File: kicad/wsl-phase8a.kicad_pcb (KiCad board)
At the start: 2 copper layers, 100 x 100 mm, 60 parts, among them J1 5.08mm 2P TB, J10 5.08mm 2P TB, J11 5.08mm 2P TB, J2 5.08mm 2P TB, J3 5.08mm 2P TB, J4 5.08mm 2P TB, J5 5.08mm 2P TB, J6 5.08mm 2P TB, J7 5.08mm 2P TB, J8 5.08mm 2P TB, J9 5.08mm 2P TB, Q1 AO3400A, Q2 AO3400A, U1 NE555

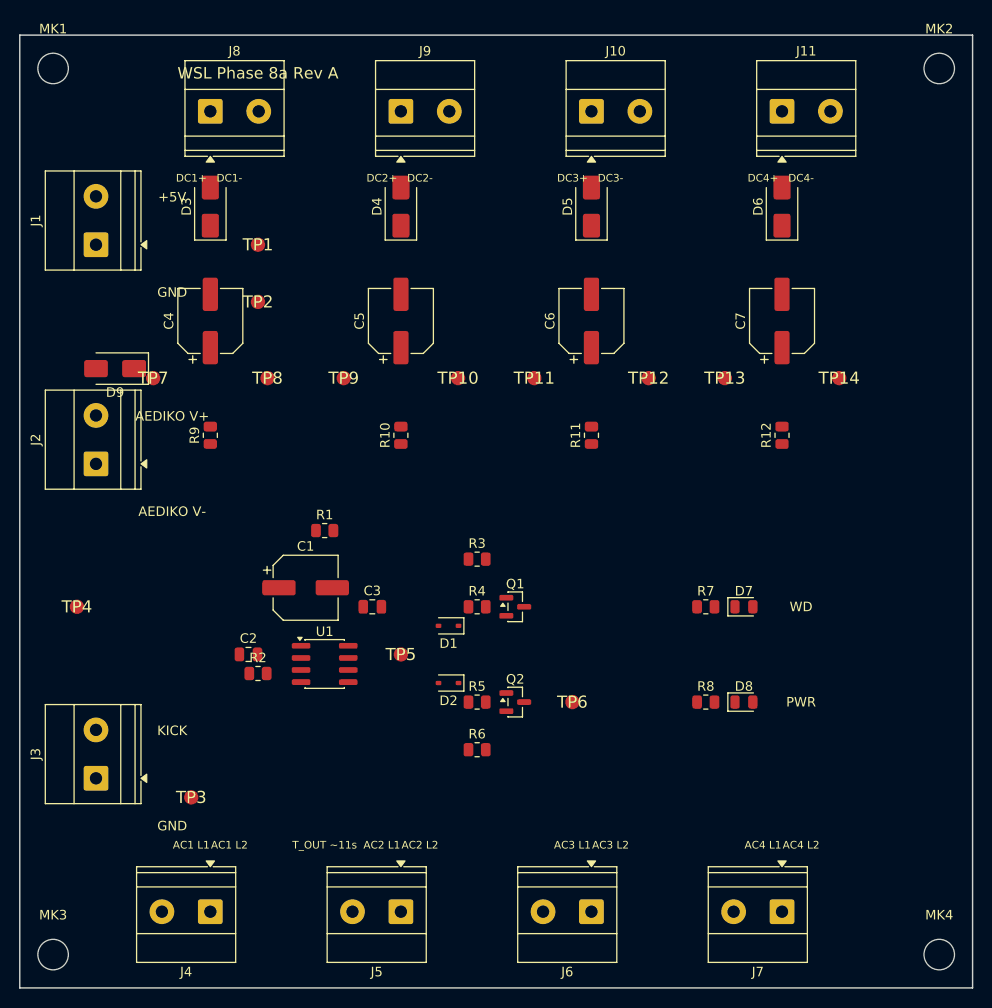
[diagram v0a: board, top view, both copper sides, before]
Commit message: Clean regen with proper TestPoint FPID + delete stale DSN/SES
Previous .ses import undid the C2 and D9 placement fixes because the
.ses file contained (place X y z) lines with the old positions. Need
to do a full DSN → autoroute → SES cycle from the CURRENT placement,
not import the stale .ses.

Also fixed test pad FPID: FootprintLoad sets only the footprint name
without the library prefix ('TestPoint_Pad_1.5x1.5mm'), which still
doesn't survive DSN export. Added explicit SetFPID with the full
'TestPoint:TestPoint_Pad_1.5x1.5mm' library:name form.

Deleted stale .dsn and .ses to force a fresh export on next run.

Co-Authored-By: Claude Opus 4.7 (1M context) <noreply@anthropic.com>
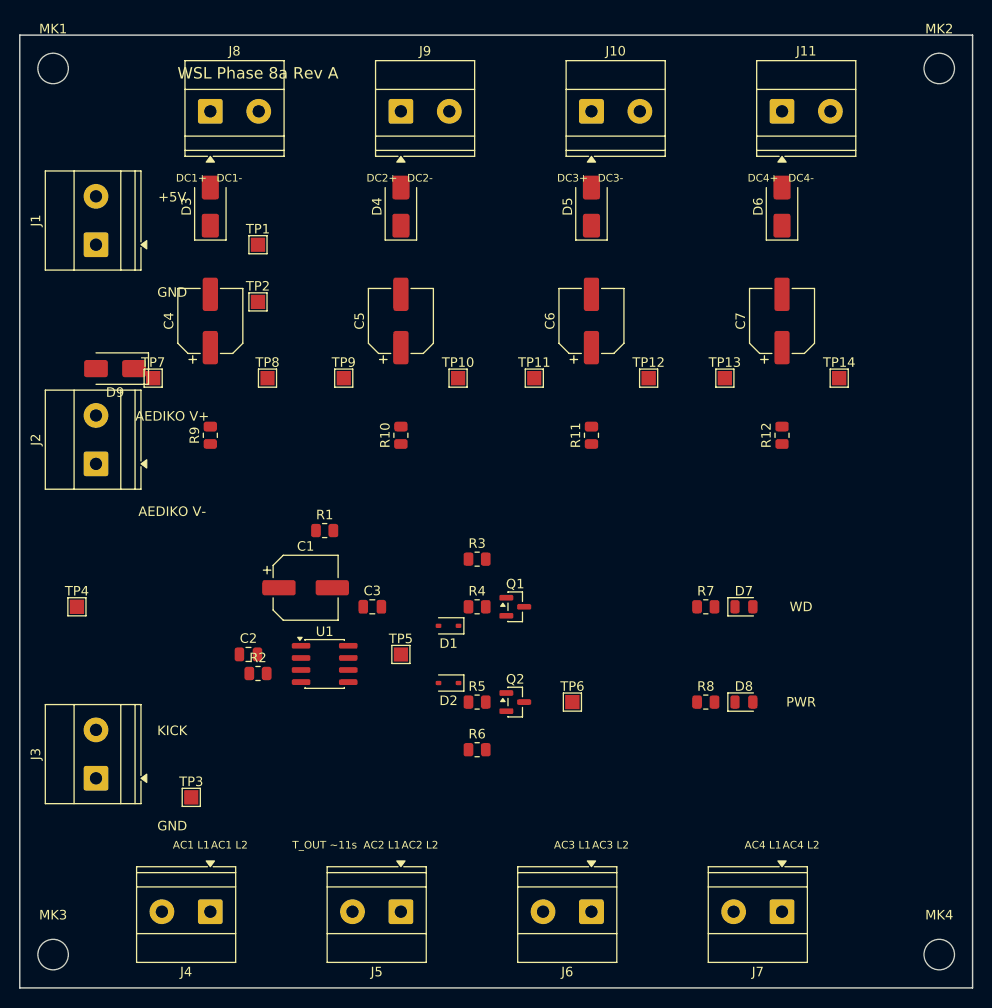
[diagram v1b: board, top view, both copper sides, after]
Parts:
- TP1, TP10, TP11, TP12, TP13, TP14, TP2, TP3, TP4, TP5, TP6, TP7, TP8, TP9: footprint custom:test_pad_1.5mm -> TestPoint:TestPoint_Pad_1.5x1.5mm

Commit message: Move channel test pads to y=48 to clear D9/J2 conflict
After D9 moved to (10, 35), TP7 at (14, 36) ended up 0mm from D9.pad1
(VCC_5V) — DRC short error. Same area had TP7 ↔ J2 courtyard overlap.

Moved all 8 channel test pads (TP7-TP14) from y=36 to y=48. That y
range is the clean gap between AC bleeders R9-R12 at y=42 and the
watchdog cluster starting at y=55+. Plenty of clearance to nearby
components.

x-positions tweaked from (14, 26, 34, 46, 54, 66, 74, 86) to
(15, 25, 35, 45, 55, 65, 75, 85) — round numbers, evenly spaced.

Co-Authored-By: Claude Opus 4.7 (1M context) <noreply@anthropic.com>
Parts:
- moved TP10 12.0 mm to (45.0, 48.0)
- moved TP11 12.0 mm to (55.0, 48.0)
- moved TP12 12.0 mm to (65.0, 48.0)
- moved TP13 12.0 mm to (75.0, 48.0)
- moved TP14 12.0 mm to (85.0, 48.0)
- moved TP7 12.0 mm to (15.0, 48.0)
- moved TP8 12.0 mm to (25.0, 48.0)
- moved TP9 12.0 mm to (35.0, 48.0)

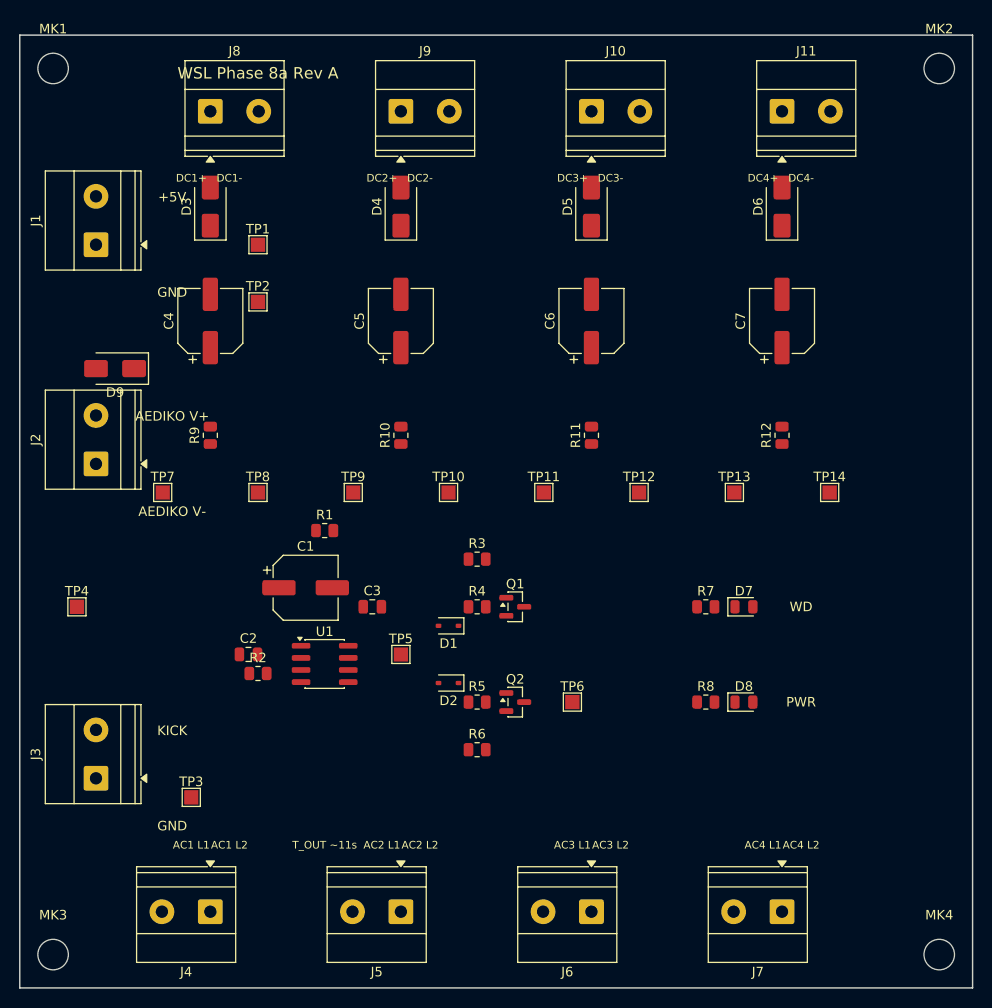
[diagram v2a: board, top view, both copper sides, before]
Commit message: Silkscreen polish: consolidate per-pin labels to per-channel
Was 26 labels with many pairs too close together (KiCad's silk-min-width
constraint flagged AC1 L1/L2, AC2 L1/L2, etc. for being 4mm apart when
5mm is the minimum). Title and power-terminal labels were overlapping
J1/J2/J8 footprint outlines too.

Cut to 13 labels:
- Removed individual DC1+ / DC1- / AC1 L1 / AC1 L2 pairs
- Replaced with single 'CH1 DC' (top) and 'CH1 24VAC' (bottom) labels
  per channel — pin numbers on the terminal outline already show polarity
- Consolidated power terminal labels: '+5V/GND', 'AEDIKO', 'KICK/GND'
  next to J1, J2, J3 (was 6 separate labels for the 3 terminals)
- Removed 'WSL Phase 8a Rev A' title (was overlapping J8) and the
  'T_OUT ~11s' service note (overlapping U1 area)

Expected DRC reduction: 22 -> ~5 warnings (a few residual silk_over_copper
warnings on test pad refdes will remain, those are unavoidable for the
TestPoint footprint since the refdes sits over its own pad).

Co-Authored-By: Claude Opus 4.7 (1M context) <noreply@anthropic.com>
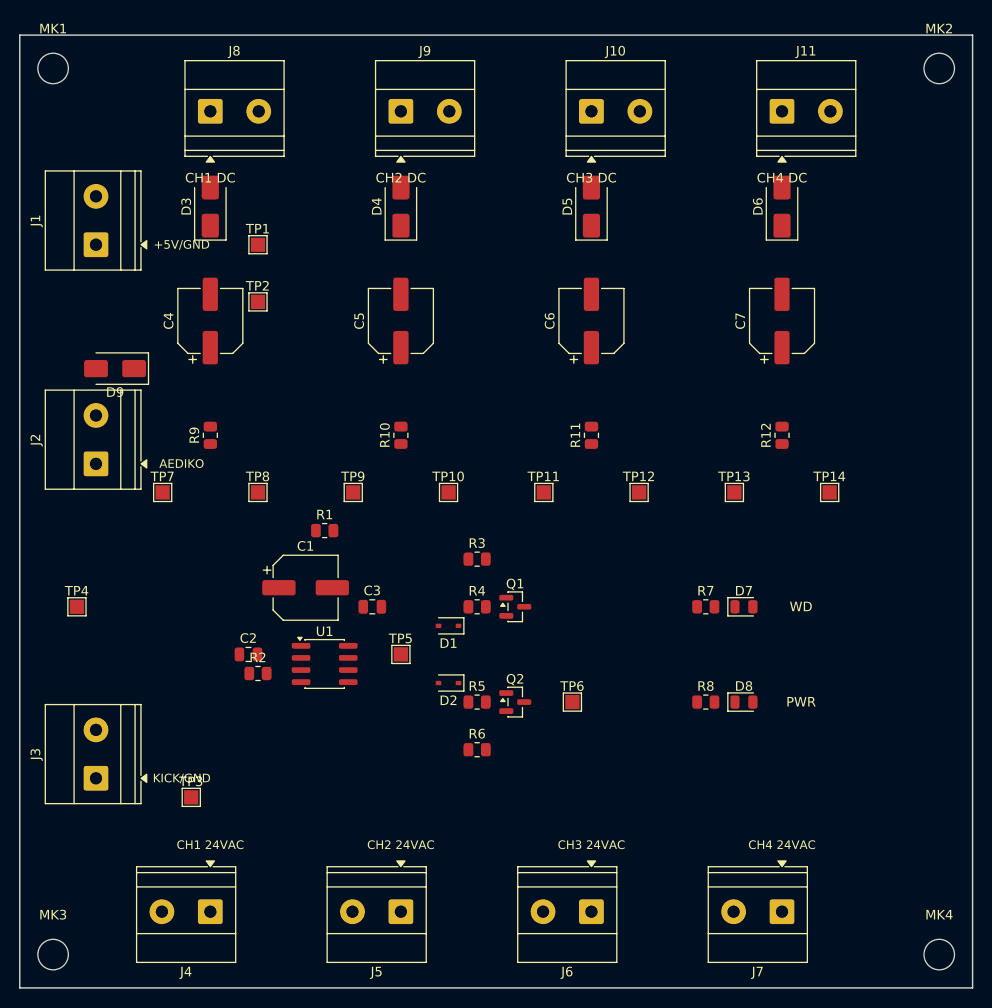
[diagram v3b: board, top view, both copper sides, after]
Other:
- board text added: "+5V/GND"
- board text added: "AEDIKO"
- board text added: "CH1 24VAC"
- board text added: "CH1 DC"
- board text added: "CH2 24VAC"
- board text added: "CH2 DC"
- board text added: "CH3 24VAC"
- board text added: "CH3 DC"
- board text added: "CH4 24VAC"
- board text added: "CH4 DC"
- board text added: "KICK/GND"
- board text removed: "+5V"
- board text removed: "AC1 L1"
- board text removed: "AC1 L2"
- board text removed: "AC2 L1"
- board text removed: "AC2 L2"
- board text removed: "AC3 L1"
- board text removed: "AC3 L2"
- board text removed: "AC4 L1"
- board text removed: "AC4 L2"
- board text removed: "AEDIKO V+"
- board text removed: "AEDIKO V-"
- board text removed: "DC1+"
- board text removed: "DC1-"
- board text removed: "DC2+"
- board text removed: "DC2-"
- board text removed: "DC3+"
- board text removed: "DC3-"
- board text removed: "DC4+"
- board text removed: "DC4-"
- board text removed: "GND"
- board text removed: "KICK"
- board text removed: "T_OUT ~11s"
- board text removed: "WSL Phase 8a Rev A"

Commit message: Add U1.pin8 -> C2.pin1 VCC track FreeRouting missed
FreeRouting routed VCC_5V to all pads except U1.pin8, leaving the
NE555's VCC pin unconnected. Single DRC error, otherwise board is
clean.

scripts/fix_u1_vcc.py adds a 3-segment L-shaped track on F.Cu at
0.5mm width (Power net class):
  U1.pin8 (34.475, 64.095)
   -> UP to (34.475, 62.0)         [clears U1 body top at y=63.55]
   -> LEFT to (23.05, 62.0)        [horizontal above U1]
   -> DOWN to C2.pin1 (23.05, 65)  [tied into existing VCC net]

Operates on the routed .kicad_pcb directly; does not regen or wipe
FreeRouting's traces.

Co-Authored-By: Claude Opus 4.7 (1M context) <noreply@anthropic.com>
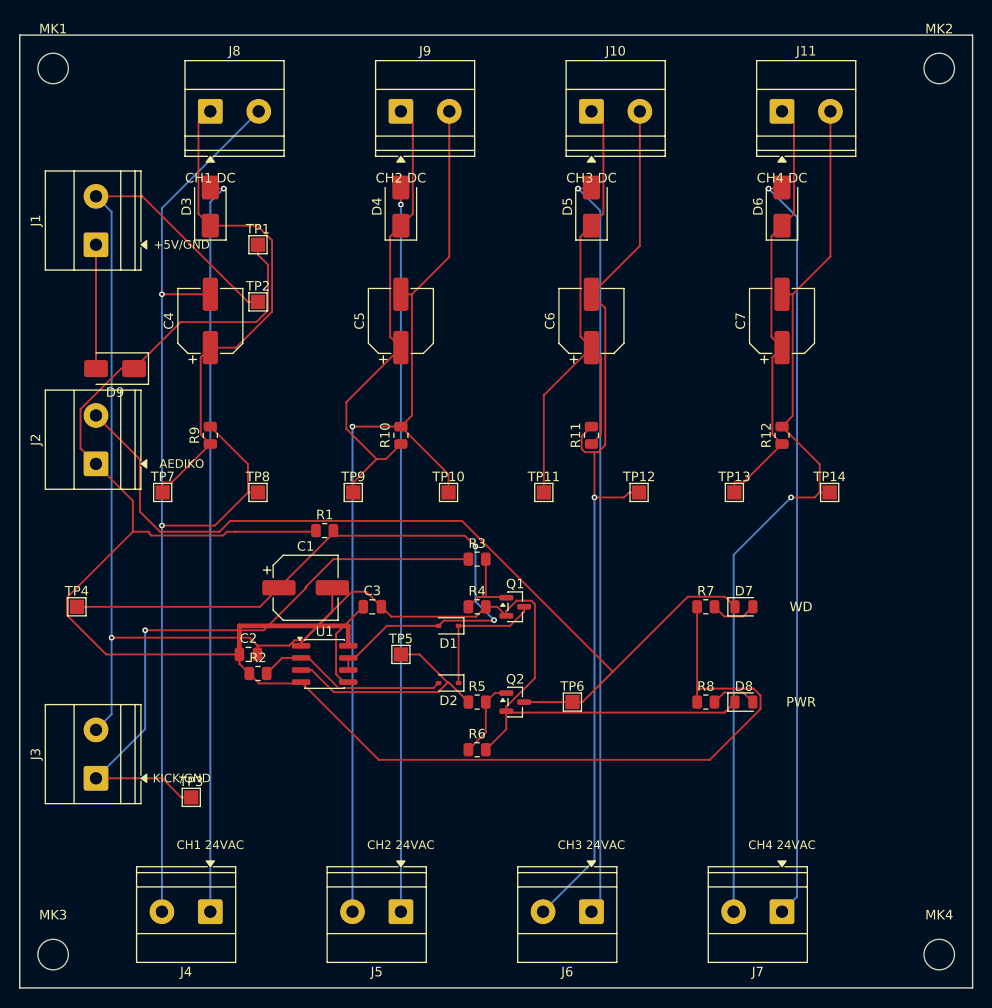
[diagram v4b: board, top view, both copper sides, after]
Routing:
- net VCC_5V: track 0.00 -> 194.7 mm
- net GND: track 0.00 -> 179.3 mm, vias 0 -> 1
- net CH1_RETURN: track 0.00 -> 113.4 mm, vias 0 -> 2
- net CH2_RETURN: track 0.00 -> 101.3 mm, vias 0 -> 1
- net CH3_RETURN: track 0.00 -> 98.8 mm, vias 0 -> 1
- net COIL_GND_RETURN: track 0.00 -> 96.7 mm
- net CH4_RETURN: track 0.00 -> 95.1 mm, vias 0 -> 1
- net AC_CH4_L1: track 0.00 -> 79.2 mm, vias 0 -> 1
- net AC_CH3_L1: track 0.00 -> 78.7 mm, vias 0 -> 1
- net AC_CH1_L1: track 0.00 -> 77.9 mm, vias 0 -> 1
- net AC_CH2_L1: track 0.00 -> 76.0 mm, vias 0 -> 1
- net TIMING_NODE: track 0.00 -> 72.7 mm, vias 0 -> 2
- net KICK: track 0.00 -> 65.6 mm, vias 0 -> 1
- net DC_CH3_POS: track 0.00 -> 55.0 mm
- net DC_CH1_POS: track 0.00 -> 54.4 mm
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
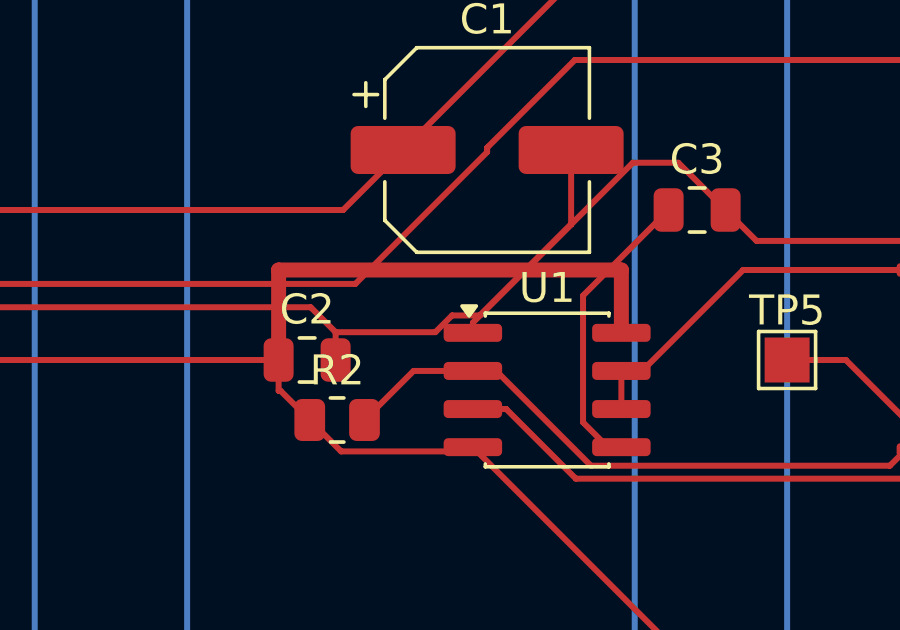
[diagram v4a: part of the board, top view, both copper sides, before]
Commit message: Remove bad U1.pin8 VCC tracks; manual interactive route needed
My fix_u1_vcc.py routed VCC at y=62 which crossed multiple existing
F.Cu traces (KICK, GND, NE555_CTRL — all run through that y range).
Added 7 new DRC errors. Programmatic routing without knowing the
existing trace layout is unsafe; KiCad's push-and-shove interactive
router handles obstacles correctly.

undo_u1_vcc_fix.py removes the 3 bad track segments by matching their
endpoint coordinates exactly. Board back to its state from FreeRouting
import (1 unconnected error: U1.pin8 VCC).

Next: manual route in KiCad with X tool.

Co-Authored-By: Claude Opus 4.7 (1M context) <noreply@anthropic.com>
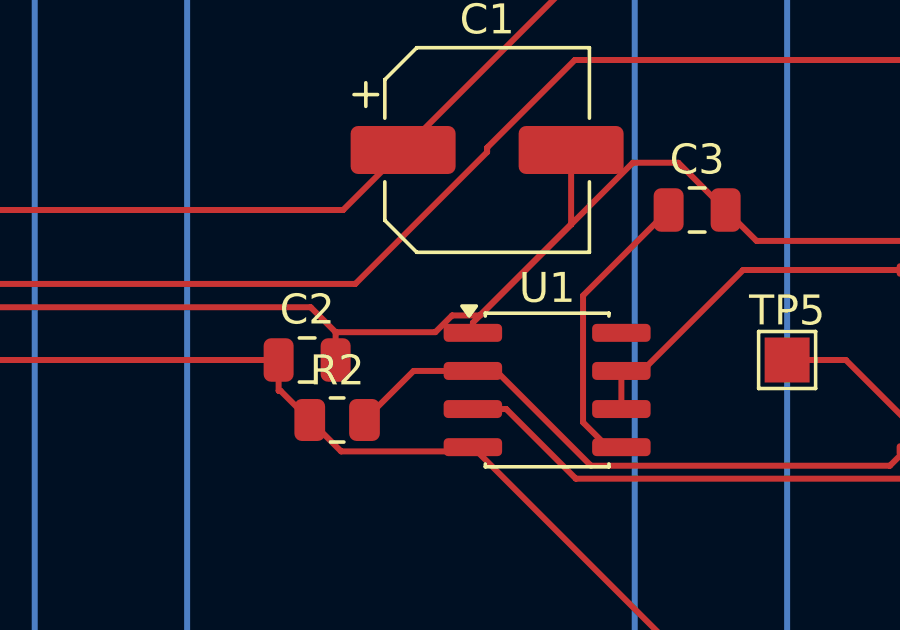
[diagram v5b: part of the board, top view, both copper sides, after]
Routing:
- net VCC_5V: track 194.7 -> 178.1 mm
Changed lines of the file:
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@@
-	)
-	(segment
-		(start 34.475 64.095)
-		(end 34.475 62)
-		(width 0.5)
-		(layer "F.Cu")
-		(net "VCC_5V")
 	)
 	(segment
@@
 		(end 29.525 67.905)
 		(width 0.2)
-		(layer "F.Cu")
-		(net "VCC_5V")
-	)
-	(segment
-		(start 34.475 62)
-		(end 23.05 62)
-		(width 0.5)
 		(layer "F.Cu")
 		(net "VCC_5V")
@@
 		(layer "F.Cu")
 		(net "VCC_5V")
-	)
-	(segment
-		(start 23.05 62)
-		(end 23.05 65)
-		(width 0.5)
-		(layer "F.Cu")
-		(net "VCC_5V")

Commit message: rev-C respin + board-#1 bring-up + 2026-06-27 machine metering + Fable review
- relay footprint root-cause fix in generate_kicad_netlist_revB.py (coil 2&5 /
  COM 1 / NO 3 / NC 4 unused, bench-metered) + full PCB toolchain + fab tree
  as ordered at JLCPCB (qty 5)
- rev-B board #1 bench bring-up docs, test packets, rev-C change list +
  readiness checklist (gates G1-G5)
- Section F machine-harness spec, metering guide, device location guide
- at-machine metering results: SC=C2A-U, TB=interlock-only (no cavity),
  N=motion-cam common, grippers GS1-7,9,10 cavities, PBZ=EE, BS=CC
- Fable review 2026-06-27: 62 verified findings incl. CRITICAL J_SAFETY
  TB/SC loop unbuildable as measured (docs/phase8_fable_review_2026-06-27.md)

Co-Authored-By: Claude Fable 5 <noreply@anthropic.com>
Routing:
- net VCC_5V: track 178.1 -> 193.3 mm, vias 0 -> 2
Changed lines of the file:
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@@
 			(plotframeref no)
 			(mode 1)
-			(useauxorigin no)
+			(useauxorigin yes)
 			(pdf_front_fp_property_popups yes)
 			(pdf_back_fp_property_popups yes)
@@
 			(outputformat 1)
 			(mirror no)
-			(drillshape 1)
+			(drillshape 0)
 			(scaleselection 1)
-			(outputdirectory "")
+			(outputdirectory "gerbers/")
 		)
 	)
@@
 			(at 2.54 -6.32 90)
 			(layer "F.SilkS")
+			(hide yes)
 			(effects
 				(font
@@
 			(at 0 -1.648 0)
 			(layer "F.SilkS")
+			(hide yes)
 			(effects
 				(font
@@
 			(at 0 -2.5 180)
 			(layer "F.SilkS")
+			(hide yes)
 			(effects
 				(font
@@
 			(at 0 -1.65 0)
 			(layer "F.SilkS")
+			(hide yes)
 			(effects
 				(font
@@
 		(layer "Edge.Cuts")
 	)
-	(gr_text "+5V/GND"
-		(at 17 22 0)
+	(gr_text "AEDIKO"
+		(at 17 45 0)
 		(layer "F.SilkS")
 		(effects
@@
 		)
 	)
-	(gr_text "AEDIKO"
-		(at 17 45 0)
+	(gr_text "CH1 24VAC"
+		(at 20 85 0)
 		(layer "F.SilkS")
 		(effects
@@
 		)
 	)
-	(gr_text "KICK/GND"
-		(at 17 78 0)
+	(gr_text "CH2 24VAC"
+		(at 40 85 0)
 		(layer "F.SilkS")
 		(effects
@@
 		)
 	)
-	(gr_text "CH1 24VAC"
-		(at 20 85 0)
+	(gr_text "CH3 24VAC"
+		(at 60 85 0)
 		(layer "F.SilkS")
 		(effects
@@
 		)
 	)
-	(gr_text "CH2 24VAC"
-		(at 40 85 0)
+	(gr_text "CH4 24VAC"
+		(at 80 85 0)
 		(layer "F.SilkS")
 		(effects
@@
 		)
 	)
-	(gr_text "CH3 24VAC"
-		(at 60 85 0)
+	(gr_text "+5V/GND"
+		(at 1.5 26 90)
 		(layer "F.SilkS")
 		(effects
@@
 		)
 	)
-	(gr_text "CH4 24VAC"
-		(at 80 85 0)
+	(gr_text "KICK/GND"
+		(at 1.5 78 90)
 		(layer "F.SilkS")
 		(effects
@@
 	)
 	(gr_text "CH1 DC"
-		(at 20 15 0)
+		(at 12.5 12.5 0)
 		(layer "F.SilkS")
 		(effects
@@
 	)
 	(gr_text "CH2 DC"
-		(at 40 15 0)
+		(at 32.5 12.5 0)
 		(layer "F.SilkS")
 		(effects
@@
 	)
 	(gr_text "CH3 DC"
-		(at 60 15 0)
+		(at 52.5 12.5 0)
 		(layer "F.SilkS")
 		(effects
@@
 	)
 	(gr_text "CH4 DC"
-		(at 80 15 0)
+		(at 72.5 12.5 0)
 		(layer "F.SilkS")
 		(effects
@@
 	)
 	(segment
+		(start 34.475 64.095)
+		(end 35.6 62.8)
+		(width 0.3)
+		(layer "F.Cu")
+		(net "VCC_5V")
+	)
+	(segment
 		(start 71.0875 68.5862)
 		(end 77.0131 68.5862)
@@
 		(net "VCC_5V")
 	)
+	(via
+		(at 35.6 62.8)
+		(size 0.6)
+		(drill 0.3)
+		(layers "F.Cu" "B.Cu")
+		(net "VCC_5V")
+	)
+	(via
+		(at 37.6813 76.0613)
+		(size 0.6)
+		(drill 0.3)
+		(layers "F.Cu" "B.Cu")
+		(net "VCC_5V")
+	)
+	(segment
+		(start 35.6 62.8)
+		(end 37.6813 76.0613)
+		(width 0.3)
+		(layer "B.Cu")
+		(net "VCC_5V")
+	)
